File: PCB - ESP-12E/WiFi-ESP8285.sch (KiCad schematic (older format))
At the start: 24 parts, among them SW2 B3U-1000P, T1 1909763-1, U4 ESP8285, X3 FA-128_26.0000MF10Z-AC3

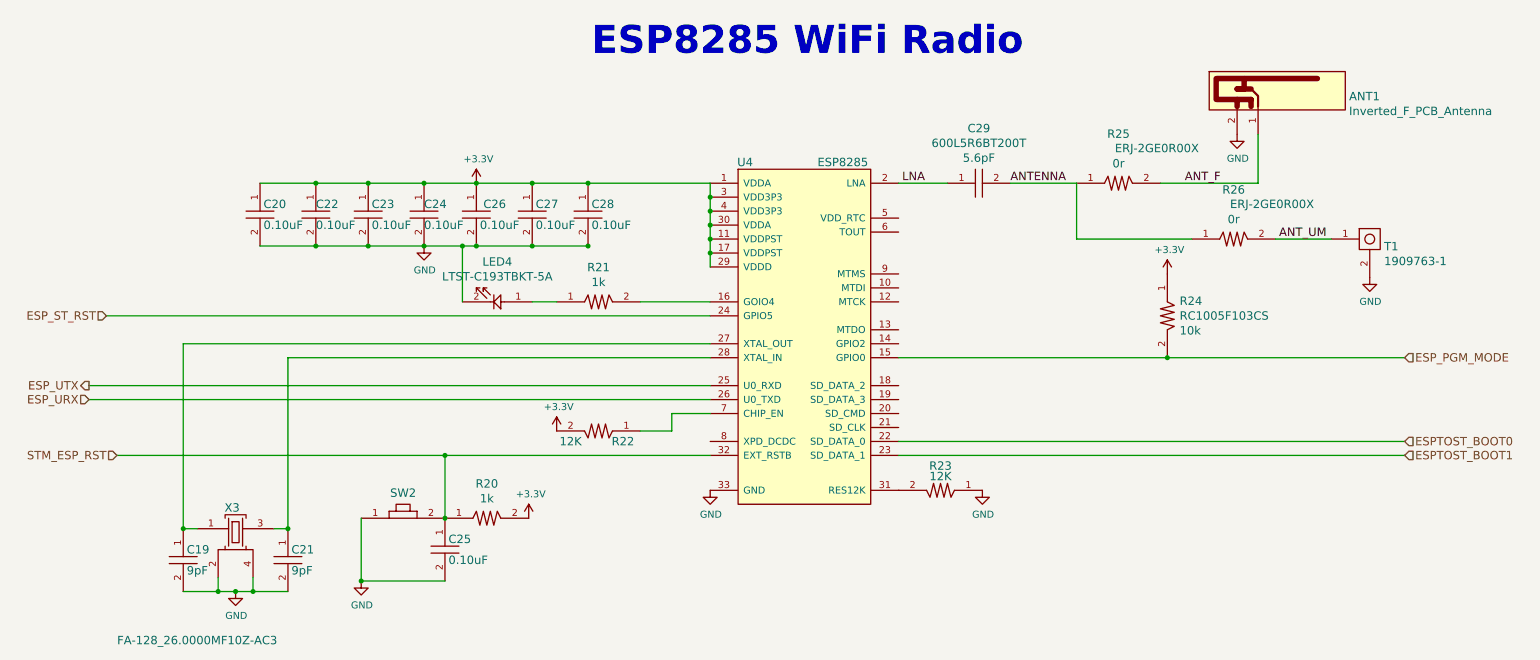
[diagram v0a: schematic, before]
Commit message: DRC Cleared and Pictures
DRC cleared of errors for both Aria board designs. New pictures have
been added. Readme has also been updated.
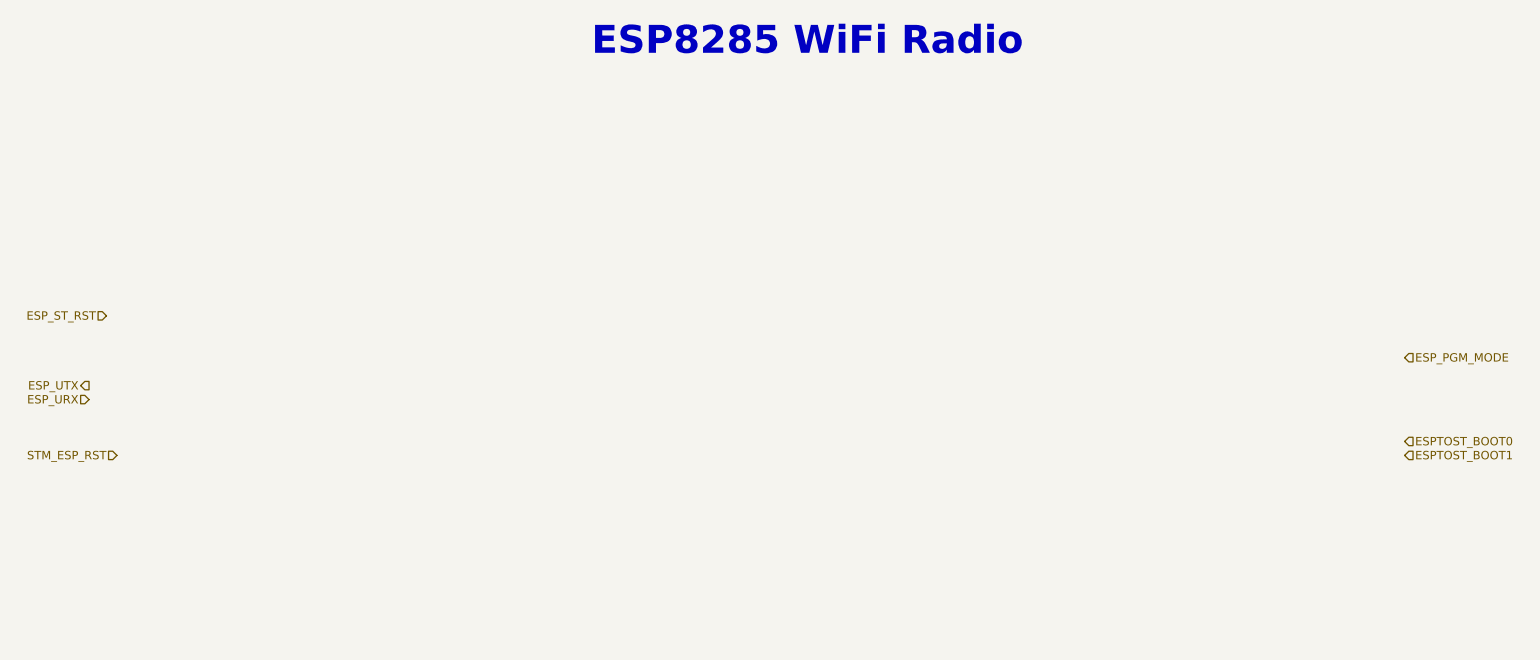
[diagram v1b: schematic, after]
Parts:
- removed ANT1: Inverted_F_PCB_Antenna, PCB_Footprints:PCB_IF_ANT_2.4G, symbol Inverted_F_PCB_Antenna
- removed C19, C21: CL05C090CB5NNNC, PCB_Footprints:C0402, symbol CL05C090CB5NNNC
- removed C20, C22, C23, C24, C25, C26, C27, C28: CL05B104JP5NNNC, PCB_Footprints:C0402, symbol CL05B104JP5NNNC
- removed C29: 600L5R6BT200T, PCB_Footprints:C0402, symbol 600L5R6BT200T
- removed LED4: LTST-C193TBKT-5A, PCB_Footprints:LED0603, symbol LTST-C193TBKT-5A
- removed R20, R21: RC1005F102CS, PCB_Footprints:R0402, symbol RC1005F102CS
- removed R22, R23: RC1005F123CS, PCB_Footprints:R0402, symbol RC1005F123CS
- removed R24: RC1005F103CS, PCB_Footprints:R0402, symbol RC1005F103CS
- removed R25, R26: ERJ-2GE0R00X, PCB_Footprints:R0402, symbol ERJ-2GE0R00X
- removed SW2: B3U-1000P, PCB_Footprints:B3U-1000P, symbol B3U-1000P
- removed T1: 1909763-1, PCB_Footprints:1909763-1, symbol 1909763-1
- removed U4: ESP8285, PCB_Footprints:ESP8285, symbol ESP8285
- removed X3: FA-128_26.0000MF10Z-AC3, PCB_Footprints:FA-128_26.0000MF10Z-AC3, symbol FA-128_26.0000MF10Z-AC3
